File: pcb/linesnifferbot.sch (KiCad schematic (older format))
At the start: 1 part

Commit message: Created some new library files and started work on schematic
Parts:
- removed ME?: PololMororEncodr, symbol PololMororEncodr
- added BT?: RN42, symbol RN42
- added D?: BT_CON, symbol LED
- added D?: BT_STAT, symbol LED
- added JP?: F_RST, symbol Jumper_NO_Small
- added JP?: F_BAUD, symbol Jumper_NO_Small
- added ME? (x2): PololuMotoEncoder, symbol PololuMotoEncoder
- added R? (x2): R, symbol R
- added U? (x2): DRV8870, symbol DRV8870
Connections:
- net labels added: +3.3V, GND
- wire segments 0 -> 37
- no-connect marks 0 -> 19

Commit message: Moving along...
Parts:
- added BT?: Battery, symbol Battery
- added C?: CP, symbol CP
- added JP?: ENC_INT/I2C_SCL, symbol Jumper_NC_Dual
- added JP?: ENC_INT/I2C_SDA, symbol Jumper_NC_Dual
- added Q?: Q_NMOS_DGS, symbol Q_NMOS_DGS
- added R? (x8): 10k, symbol R
- added R? (x2): 70R, symbol R
- added R? (x2): 0R18, symbol R
- added R?: SHUNT, symbol R
- added R?: 130R, symbol R
- added S? (x8): QRE1113, symbol QRE1113
- added U?: Arduino_MICRO, symbol Arduino_MICRO
- added U?: INA219, symbol INA219
- R? (x2): value R -> 330R
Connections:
- net +3V3: now also U?.4 (VREF), U?.4 (VREF)
- net GND: now also ME?.6 (GND), ME?.6 (GND), U?.1 (GND), U?.1 (GND), U?.9 (PAD), U?.9 (PAD), BT?.2 (-), C?.2, Q?.3 (S), R?.1, R?.1, S?.4, S?.4, S?.4, S?.4, S?.4, S?.4, S?.4, S?.4, U?.1 (A1), U?.2 (A0), U?.3 (SDA), U?.31 (GND), U?.6 (GND)
- net at U?.2 (IN2): now also U?.11 (6(PWM)/A7)
- net at U?.3 (IN1): now also U?.10 (5(PWM))
- net +BATT: now reaches U?.5 (VM)
- net +BATT: now also U?.5 (VM)
- net at U?.7 (ISEN): now also R?.2 (x2)
- net at U?.2 (IN2): now also U?.15 (10(PWM)/A10)
- net at U?.3 (IN1): now also U?.14 (9(PWM)/A9)
- net +5V: now reaches ME?.3 (VCC)
- net +5V: now also ME?.3 (VCC), R?.1, R?.1, R?.1, R?.1, R?.1, R?.1, R?.1, R?.1, R?.1, R?.1, R?.1, U?.29 (5V), U?.5 (VS)
- net at ME?.4 (A): now also U?.16 (11(PWM))
- net at ME?.5 (B): now also JP?.3 (x2)
- net at ME?.4 (A): now also U?.17 (12/A11)
- net at BT?.13 (UART_RX): now also U?.3 (1(INT)/TX)
- net at BT?.14 (UART_TX): now also U?.4 (0(INT)/RX)
- new net: R?.2, S?.3, U?.13 (8/A8)
- new net: R?.2, S?.3, U?.21 (A0)
- new net: R?.2, S?.3, U?.22 (A1)
- new net: R?.2, S?.3, U?.23 (A2)
- new net: R?.2, S?.3, U?.24 (A3)
- new net: R?.2, S?.3, U?.25 (A4)
- new net: R?.2, S?.3, U?.26 (A5)
- new net: JP?.2, U?.7 (2(INT)/SDA)
- new net: JP?.2, U?.8 (3(PWM,INT)/SCL)
- new net: R?.2, S?.3, U?.9 (4/A6)
- new net: S?.1, S?.2 (x5)
- new net: Q?.1 (D), S?.2, S?.2, S?.2
- new net: R?.2, S?.1 (x3)
- new net: BT?.1 (+), C?.1, R?.1, U?.8 (IN+)
- new net: R?.2, U?.7 (IN-)
- no-connect marks 19 -> 29
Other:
- moved on the sheet: BT?, D?, JP?, ME?, R?, U?

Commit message: Updated schematic, geting closer to final form
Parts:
- removed BT?: Battery, symbol Battery
- removed C?: CP, symbol CP
- removed JP?: ENC_INT/I2C_SCL, symbol Jumper_NC_Dual
- removed JP?: ENC_INT/I2C_SDA, symbol Jumper_NC_Dual
- removed R?: SHUNT, symbol R
- removed U?: INA219, symbol INA219
- added BT?: Battery, symbol Battery
- added C?: 1uF, symbol CP
- added C?: 10uF, symbol CP
- added C?: 4.7uF, symbol CP
- added C? (x2): 100nF, symbol C_Small
- added D?: POWER, symbol LED
- added D?: STATUS, symbol LED
- added J? (x4): GS3, Connectors:GS3, symbol GS3
- added J? (x2): GS2, Connectors:GS2, symbol GS2
- added R?: R, symbol R
- added R? (x7): 10k, symbol R
- added R? (x2): 560R, symbol R
- added SW?: SPDT, symbol SPDT
- added SW?: BTN, symbol BTN
- added U? (x2): NC7SZ86, symbol NC7SZ86
- added U?: 74HC74_, symbol 74HC74_
- added U?: CD4051B, symbol CD4051B
- added U?: INA139, symbol INA139
- added U?: MCP1703, symbol MCP1703
- added U?: NCP5501DT50, symbol NCP5501DT50
- added U?: TXB0104, symbol TXB0104
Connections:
- net +3V3: now also C?.1, C?.1, R?.1, R?.1, U?.1 (VCCA), U?.3 (OUT), U?.8 (OE)
- net +5V: now also C?.1, C?.2, R?.1, R?.1, R?.2, SW?.1 (A), U?.1 (!R1), U?.1 (IN), U?.10 (!S2), U?.13 (!R2), U?.14 (VCC), U?.14 (VCCB), U?.16 (VDD), U?.3 (OUT), U?.4 (!S1), U?.5 (VCC), U?.5 (VCC)
- net +BATT: now also R?.1, R?.2, SW?.3 (B), U?.3 (V_IN+), U?.5 (V+); no longer U?.5 (VM), U?.5 (VM)
- net GND: now also R?.1, R?.1, BT?.2 (-), C?.1, C?.2, C?.2, C?.2, C?.2, D?.1 (K), D?.1 (K), R?.2, R?.2, U?.2 (GND), U?.2 (GND), U?.2 (GND), U?.3 (GND), U?.3 (GND), U?.4 (GND), U?.4 (PAD), U?.6 (INH), U?.7 (GND), U?.7 (GND), U?.7 (VEE), U?.8 (VSS); no longer R?.2, R?.2
- net at U?.2 (IN2): now also U?.14 (9(PWM)/A9); no longer U?.11 (6(PWM)/A7)
- net at U?.3 (IN1): now also U?.15 (10(PWM)/A10); no longer U?.10 (5(PWM))
- net at U?.2 (IN2): now also U?.10 (5(PWM)); no longer U?.15 (10(PWM)/A10)
- net at U?.3 (IN1): now also U?.11 (6(PWM)/A7); no longer U?.14 (9(PWM)/A9)
- net at ME?.4 (A): now also U?.1 (A), U?.2 (D1); no longer U?.16 (11(PWM))
- net at ME?.5 (B): now also U?.2 (B), U?.3 (CK1)
- net at ME?.4 (A): now also U?.1 (A), U?.12 (D2); no longer U?.17 (12/A11)
- net at ME?.5 (B): now also U?.11 (CK2), U?.2 (B)
- net at BT?.13 (UART_RX): now also U?.5 (A4); no longer U?.3 (1(INT)/TX)
- net at BT?.14 (UART_TX): now also U?.4 (A3); no longer U?.4 (0(INT)/RX)
- net at D?.1 (K): now also R?.2; no longer R?.1 (x2)
- net at U?.12 (7(INT)): now also J?.1 (G1)
- net at R?.2, S?.3: now also U?.4 (7); no longer U?.13 (8/A8)
- net at U?.18 (13(PWM)): now also R?.2, SW?.2 (B)
- net at R?.2, S?.3: now also U?.13 (0); no longer U?.21 (A0)
- net at R?.2, S?.3: now also U?.14 (1); no longer U?.22 (A1)
- net at R?.2, S?.3: now also U?.15 (2); no longer U?.23 (A2)
- net at R?.2, S?.3: now also U?.12 (3); no longer U?.24 (A3)
- net at R?.2, S?.3: now also U?.1 (4); no longer U?.25 (A4)
- net at R?.2, S?.3: now also U?.5; no longer U?.26 (A5)
- net at U?.7 (2(INT)/SDA): now also J?.1 (G1), J?.2 (G2)
- net at U?.8 (3(PWM,INT)/SCL): now also J?.1 (G1), J?.2 (G2)
- net at R?.2, S?.3: now also U?.2 (6); no longer U?.9 (4/A6)
- net at Q?.2 (G): now also U?.9 (4/A6)
- new net: J?.1 (G1), U?.13 (8/A8)
- new net: U?.16 (11(PWM)), U?.5 (Q1)
- new net: U?.17 (12/A11), U?.9 (Q2)
- new net: U?.21 (A0), U?.3 (COM)
- new net: U?.11 (A), U?.22 (A1)
- new net: U?.10 (B), U?.23 (A2)
- new net: U?.24 (A3), U?.9 (C)
- new net: R?.1, U?.1 (OUT), U?.25 (A4)
- new net: R?.1, R?.2, U?.26 (A5)
- new net: J?.3 (G3), J?.3 (G3), U?.3 (1(INT)/TX)
- new net: J?.3 (G3), J?.3 (G3), U?.4 (0(INT)/RX)
- new net: J?.2 (G2), U?.4 (Y) (x2)
- new net: J?.2 (G2), U?.11 (B3)
- new net: J?.2 (G2), U?.10 (B4)
- new net: D?.2 (A), R?.1 (x2)
- new net: BT?.1 (+), SW?.2 (COM)
- new net +9V: C?.1, R?.1, U?.1 (IN), U?.4 (V_IN-), U?.5 (VM), U?.5 (VM)
- new net I2C_SCL_3.3V: R?.2, U?.2 (A1)
- new net I2C_SCL_5V: J?.1 (G1), R?.2, U?.13 (B1)
- new net I2C_SDA_3.3V: R?.2, U?.3 (A2)
- new net I2C_SDA_5V: J?.1 (G1), R?.2, U?.12 (B2)
- no-connect marks 29 -> 30
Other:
- moved on the sheet: BT?, D?, JP?, ME?, R?, U?

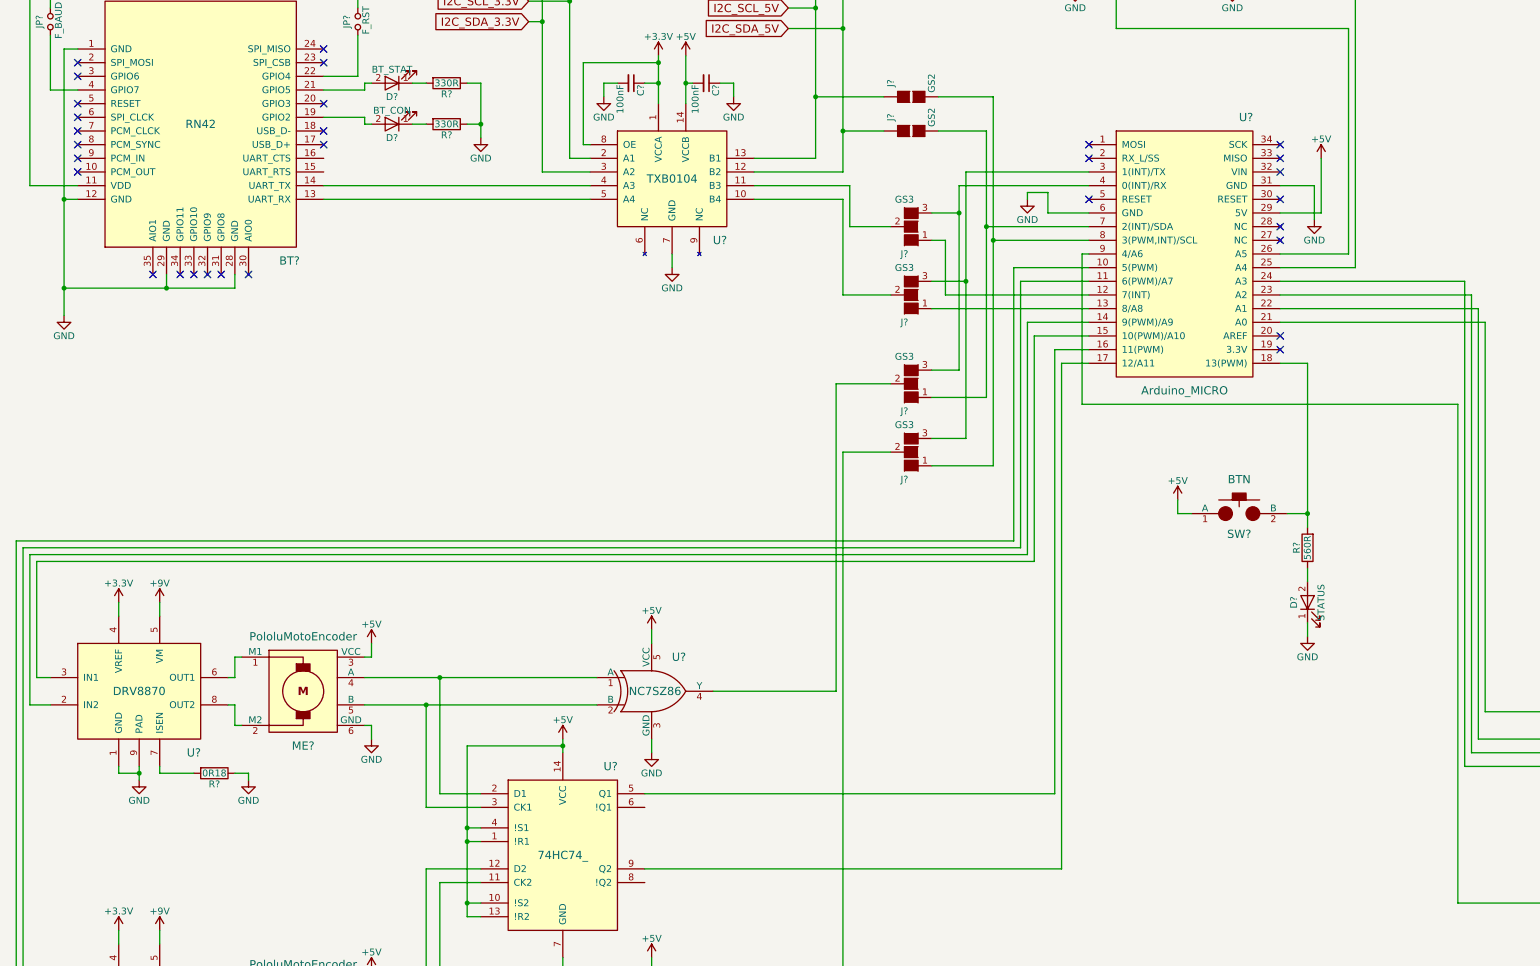
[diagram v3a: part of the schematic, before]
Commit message: Schematic: Additional LED and button
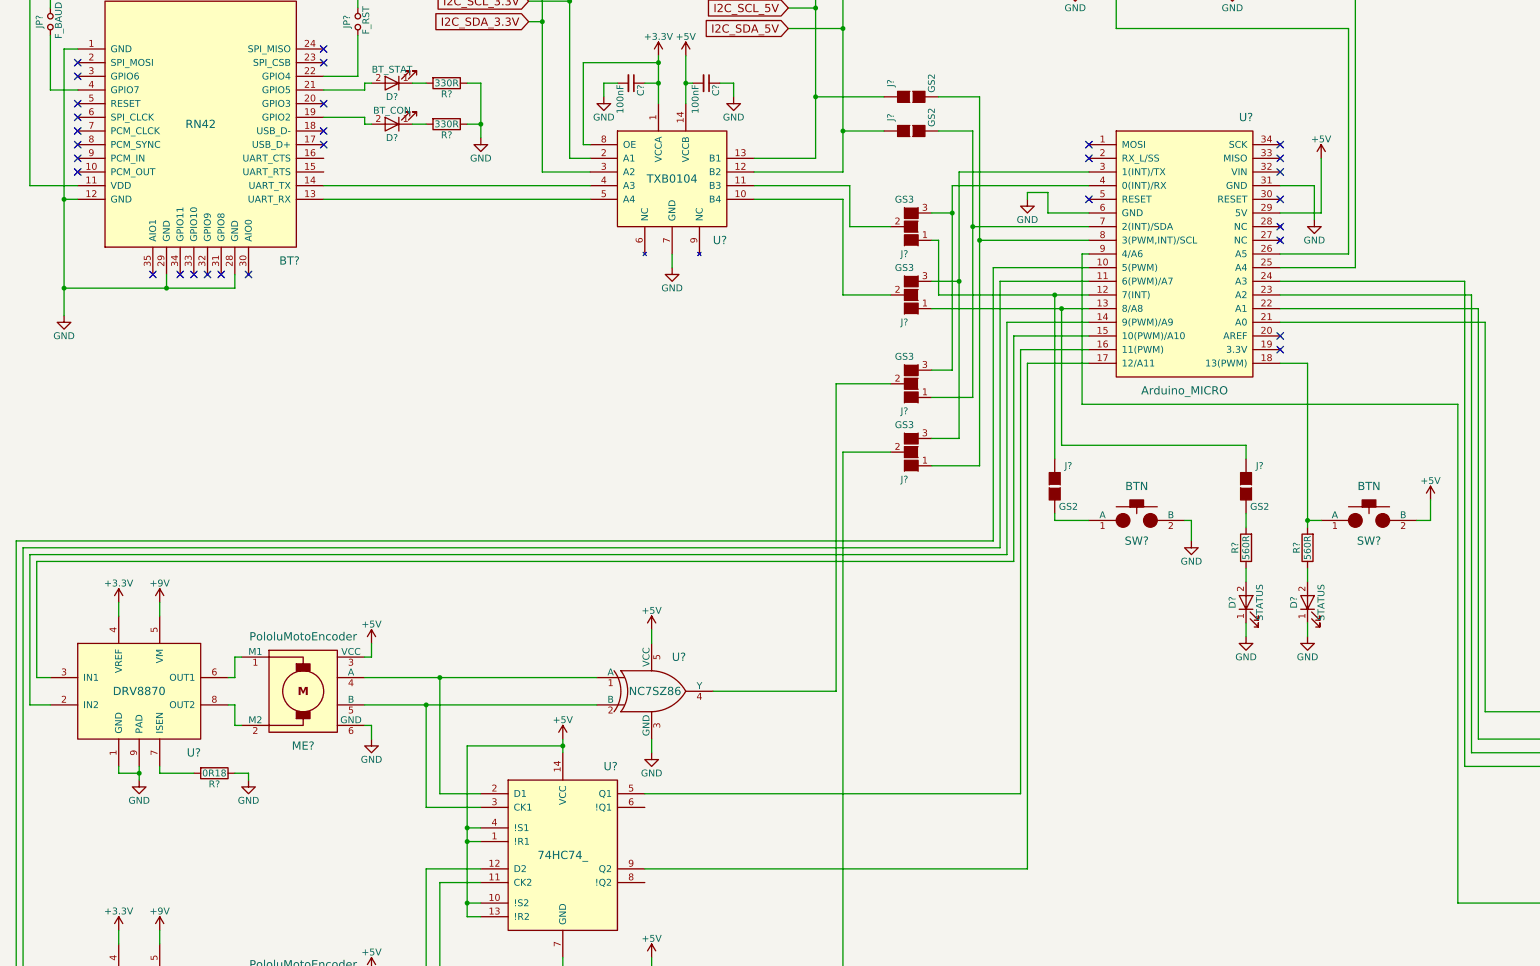
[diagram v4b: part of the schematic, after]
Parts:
- added D?: STATUS, symbol LED
- added J? (x2): GS2, Connectors:GS2, symbol GS2
- added R?: 560R, symbol R
- added SW?: BTN, symbol BTN
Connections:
- net +5V: now also SW?.2 (B); no longer SW?.1 (A)
- net GND: now also D?.1 (K), SW?.2 (B)
- net at J?.1 (G1), U?.12 (7(INT)): now also J?.1 (G1)
- net at J?.1 (G1), U?.13 (8/A8): now also J?.1 (G1)
- net at R?.2, U?.18 (13(PWM)): now also SW?.1 (A); no longer SW?.2 (B)
- new net: J?.2 (G2), R?.2
- new net: J?.2 (G2), SW?.1 (A)
- new net: D?.2 (A), R?.1
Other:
- moved on the sheet: SW?
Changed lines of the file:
@@
 L BTN SW?
 U 1 1 58C88E15
-P 9600 6400
-F 0 "SW?" H 9600 6250 60  0000 C CNN
-F 1 "BTN" H 9600 6650 60  0000 C CNN
-F 2 "" H 9600 6400 60  0001 C CNN
-F 3 "" H 9600 6400 60  0001 C CNN
-	1    9600 6400
+P 10550 6450
+F 0 "SW?" H 10550 6300 60  0000 C CNN
+F 1 "BTN" H 10550 6700 60  0000 C CNN
+F 2 "" H 10550 6450 60  0001 C CNN
+F 3 "" H 10550 6450 60  0001 C CNN
+	1    10550 6450
 	1    0    0    -1
 $EndComp
@@
 L +5V #PWR?
 U 1 1 58C89AF0
-P 9150 6300
-F 0 "#PWR?" H 9150 6150 50  0001 C CNN
-F 1 "+5V" H 9150 6440 50  0000 C CNN
-F 2 "" H 9150 6300 50  0001 C CNN
-F 3 "" H 9150 6300 50  0001 C CNN
-	1    9150 6300
+P 11000 6300
+F 0 "#PWR?" H 11000 6150 50  0001 C CNN
+F 1 "+5V" H 11000 6440 50  0000 C CNN
+F 2 "" H 11000 6300 50  0001 C CNN
+F 3 "" H 11000 6300 50  0001 C CNN
+	1    11000 6300
 	1    0    0    -1
 $EndComp
@@
 I2C_SCL_5V
 Wire Wire Line
-	7600 3900 8500 3900
+	7550 3900 8500 3900
 Wire Wire Line
 	2900 4100 4850 4100
@@
 	9900 4500 10400 4500
 Wire Wire Line
-	8300 9000 5250 9000
-Wire Wire Line
-	8300 5300 8300 9000
-Wire Wire Line
-	8500 5300 8300 5300
-Wire Wire Line
-	8250 5200 8500 5200
-Wire Wire Line
-	8250 8450 8250 5200
-Wire Wire Line
-	5250 8450 8250 8450
-Wire Wire Line
-	8100 5100 8500 5100
-Wire Wire Line
-	8100 6750 8100 5100
-Wire Wire Line
-	8050 5000 8500 5000
-Wire Wire Line
-	8050 6700 8050 5000
-Wire Wire Line
-	8000 4700 8500 4700
-Wire Wire Line
-	8000 6650 8000 4700
-Wire Wire Line
-	7950 4600 7950 6600
-Wire Wire Line
-	8500 4600 7950 4600
+	8050 9000 5250 9000
+Wire Wire Line
+	8050 5300 8050 9000
+Wire Wire Line
+	8500 5300 8050 5300
+Wire Wire Line
+	8000 5200 8500 5200
+Wire Wire Line
+	8000 8450 8000 5200
+Wire Wire Line
+	5250 8450 8000 8450
+Wire Wire Line
+	7950 5100 8500 5100
+Wire Wire Line
+	7950 6750 7950 5100
+Wire Wire Line
+	7900 5000 8500 5000
+Wire Wire Line
+	7900 6700 7900 5000
+Wire Wire Line
+	7850 4700 8500 4700
+Wire Wire Line
+	7850 6650 7850 4700
+Wire Wire Line
+	7800 4600 7800 6600
+Wire Wire Line
+	8500 4600 7800 4600
 Wire Wire Line
 	6700 10100 5750 10100
@@
 Wire Wire Line
 	5750 7700 6650 7700
-Connection ~ 7550 4200
-Connection ~ 7600 4700
-Wire Wire Line
-	7800 4400 8500 4400
-Wire Wire Line
-	7800 3350 7800 6050
-Wire Wire Line
-	7800 6050 7350 6050
-Wire Wire Line
-	7750 5550 7350 5550
-Wire Wire Line
-	7750 3600 7750 5550
-Wire Wire Line
-	8500 4300 7750 4300
-Wire Wire Line
-	7550 5350 7350 5350
-Wire Wire Line
-	7550 4000 7550 5350
-Wire Wire Line
-	7600 5850 7350 5850
+Connection ~ 7500 4200
+Connection ~ 7550 4700
+Wire Wire Line
+	7700 4400 8500 4400
+Wire Wire Line
+	7700 3350 7700 6050
+Wire Wire Line
+	7700 6050 7350 6050
+Wire Wire Line
+	7650 5550 7350 5550
+Wire Wire Line
+	7650 3600 7650 5550
+Wire Wire Line
+	8500 4300 7650 4300
+Wire Wire Line
+	7500 5350 7350 5350
+Wire Wire Line
+	7500 4000 7500 5350
+Wire Wire Line
+	7550 5850 7350 5850
 Wire Wire Line
 	7350 4900 8500 4900
 Wire Wire Line
-	7450 4800 8500 4800
-Wire Wire Line
-	7450 4400 7450 4800
-Wire Wire Line
-	7350 4400 7450 4400
-Wire Wire Line
-	7600 3900 7600 5850
-Wire Wire Line
-	7350 4700 7600 4700
-Wire Wire Line
-	7550 4000 8500 4000
-Wire Wire Line
-	7350 4200 7550 4200
+	7400 4800 8500 4800
+Wire Wire Line
+	7400 4400 7400 4800
+Wire Wire Line
+	7350 4400 7400 4400
+Wire Wire Line
+	7550 3900 7550 5850
+Wire Wire Line
+	7350 4700 7550 4700
+Wire Wire Line
+	7500 4000 8500 4000
+Wire Wire Line
+	7350 4200 7500 4200
 Wire Wire Line
 	6700 4800 7050 4800
@@
 	11400 5000 11400 7850
 Wire Wire Line
-	7950 6600 650  6600
+	7800 6600 650  6600
 Wire Wire Line
 	650  6600 650  10200
@@
 	700  6650 700  10000
 Wire Wire Line
-	700  6650 8000 6650
+	700  6650 7850 6650
 Wire Wire Line
 	750  7800 900  7800
@@
 	750  6700 750  7800
 Wire Wire Line
-	750  6700 8050 6700
+	750  6700 7900 6700
 Wire Wire Line
 	800  7600 900  7600
@@
 	800  6750 800  7600
 Wire Wire Line
-	800  6750 8100 6750
+	800  6750 7950 6750
 Wire Wire Line
 	8700 2000 8400 2000
@@
 	14050 8550 14050 8500
 Wire Wire Line
-	7750 3600 7400 3600
-Connection ~ 7750 4300
-Wire Wire Line
-	7400 3350 7800 3350
-Connection ~ 7800 4400
+	7650 3600 7400 3600
+Connection ~ 7650 4300
+Wire Wire Line
+	7400 3350 7700 3350
+Connection ~ 7700 4400
 Wire Wire Line
 	6050 4000 6750 4000
@@
 	10100 7300 10100 7200
 Wire Wire Line
-	9150 6300 9150 6400
-Wire Wire Line
-	9150 6400 9250 6400
-Wire Wire Line
-	9950 6400 10100 6400
+	11000 6300 11000 6450
+Wire Wire Line
+	11000 6450 10900 6450
+Wire Wire Line
+	10200 6450 10100 6450
 Wire Wire Line
 	10100 5300 10100 6500
 Wire Wire Line
 	9900 5300 10100 5300
-Connection ~ 10100 6400
+Connection ~ 10100 6450
 Wire Wire Line
 	6300 2700 6500 2700
@@
 	4600 2050 4600 2150
 Connection ~ 4600 2150
+$Comp
+L GS2 J?
+U 1 1 58C6AF43
+P 9650 6200
+F 0 "J?" H 9750 6350 50  0000 C CNN
+F 1 "GS2" H 9750 6051 50  0000 C CNN
+F 2 "Connectors:GS2" V 9724 6200 50  0001 C CNN
+F 3 "" H 9650 6200 50  0001 C CNN
+	1    9650 6200
+	1    0    0    -1
+$EndComp
+$Comp
+L GS2 J?
+U 1 1 58C6B112
+P 8250 6200
+F 0 "J?" H 8350 6350 50  0000 C CNN
+F 1 "GS2" H 8350 6051 50  0000 C CNN
+F 2 "Connectors:GS2" V 8324 6200 50  0001 C CNN
+F 3 "" H 8250 6200 50  0001 C CNN
+	1    8250 6200
+	1    0    0    -1
+$EndComp
+Wire Wire Line
+	8250 6000 8250 4800
+Connection ~ 8250 4800
+Wire Wire Line
+	8300 4900 8300 5900
+Wire Wire Line
+	8300 5900 9650 5900
+Wire Wire Line
+	9650 5900 9650 6000
+Connection ~ 8300 4900
+$Comp
+L R R?
+U 1 1 58C6BFF5
+P 9650 6650
+F 0 "R?" V 9730 6650 50  0000 C CNN
+F 1 "560R" V 9650 6650 50  0000 C CNN
+F 2 "" V 9580 6650 50  0001 C CNN
+F 3 "" H 9650 6650 50  0001 C CNN
+	1    9650 6650
+	-1   0    0    1
+$EndComp
+$Comp
+L LED D?
+U 1 1 58C6C287
+P 9650 7050
+F 0 "D?" H 9650 7150 50  0000 C CNN
+F 1 "STATUS" H 9650 6950 50  0000 C CNN
+F 2 "" H 9650 7050 50  0001 C CNN
+F 3 "" H 9650 7050 50  0001 C CNN
+	1    9650 7050
+	0    -1   -1   0
+$EndComp
+$Comp
+L GND #PWR?
+U 1 1 58C6C5EB
+P 9650 7300
+F 0 "#PWR?" H 9650 7050 50  0001 C CNN
+F 1 "GND" H 9650 7150 50  0000 C CNN
+F 2 "" H 9650 7300 50  0001 C CNN
+F 3 "" H 9650 7300 50  0001 C CNN
+	1    9650 7300
+	1    0    0    -1
+$EndComp
+Wire Wire Line
+	9650 7300 9650 7200
+Wire Wire Line
+	9650 6900 9650 6800
+Wire Wire Line
+	9650 6500 9650 6400
+$Comp
+L BTN SW?
+U 1 1 58C6D555
+P 8850 6450
+F 0 "SW?" H 8850 6300 60  0000 C CNN
+F 1 "BTN" H 8850 6700 60  0000 C CNN
+F 2 "" H 8850 6450 60  0001 C CNN
+F 3 "" H 8850 6450 60  0001 C CNN
+	1    8850 6450
+	1    0    0    -1
+$EndComp
+$Comp
+L GND #PWR?
+U 1 1 58C6D896
+P 9250 6600
+F 0 "#PWR?" H 9250 6350 50  0001 C CNN
+F 1 "GND" H 9250 6450 50  0000 C CNN
+F 2 "" H 9250 6600 50  0001 C CNN
+F 3 "" H 9250 6600 50  0001 C CNN
+	1    9250 6600
+	1    0    0    -1
+$EndComp
+Wire Wire Line
+	8250 6400 8250 6450
+Wire Wire Line
+	8250 6450 8500 6450
+Wire Wire Line
+	9200 6450 9250 6450
+Wire Wire Line
+	9250 6450 9250 6600
 $EndSCHEMATC
